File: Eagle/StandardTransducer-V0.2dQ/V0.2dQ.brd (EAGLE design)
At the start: 59.2 x 58 mm, 72 parts, among them CON1 SPI, IC2 TL072D, IC3 LP5907, IC4 LORA-RA_01_SOIC, J1 87758-0216, Q1 FDN340P, Q2 FDN340P, Q3 FDN340P, Q4 FDN340P, Q5 BSP75N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

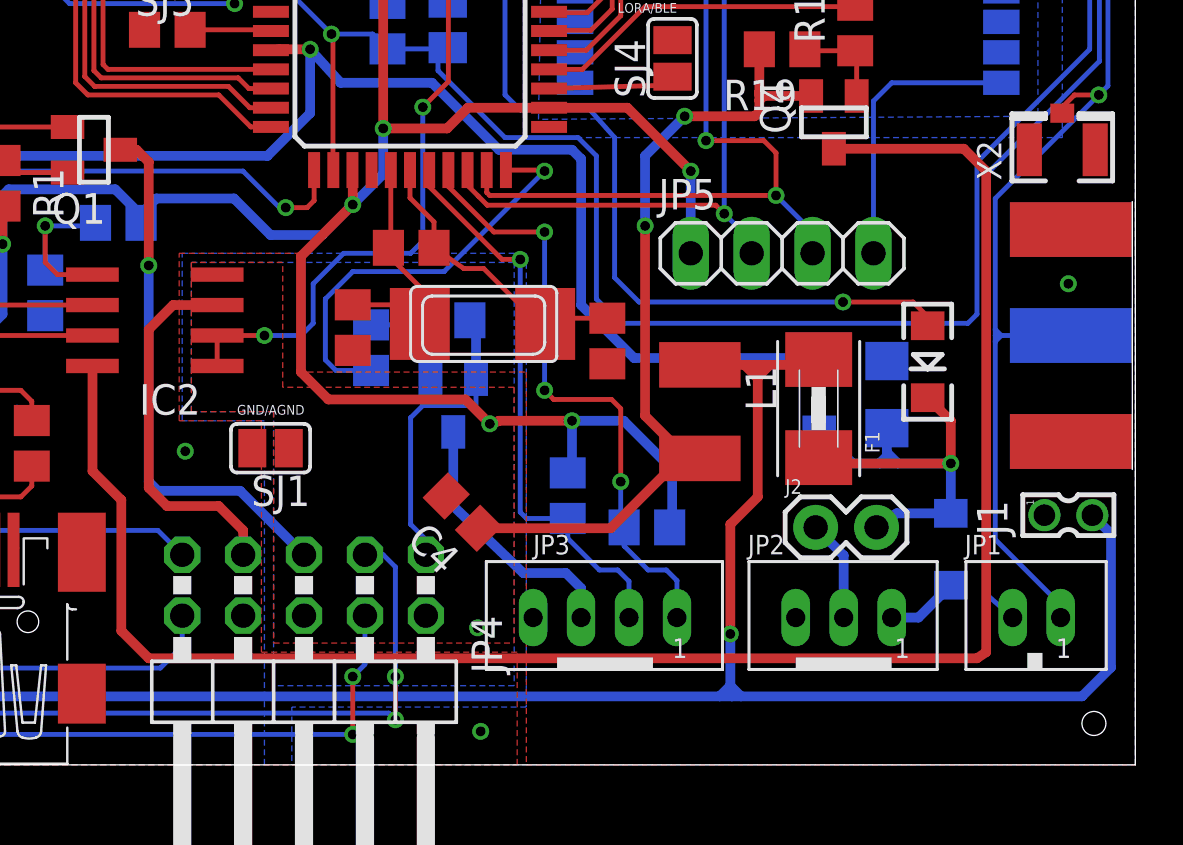
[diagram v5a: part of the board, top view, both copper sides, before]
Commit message: Update ICs, change routes and power source.
Changes made:
- BSP75 (BSP613P) to BSP75N.
- FDN 360P to FDN340P (logic level).
- LP298SX to LP5907 (250 mA).
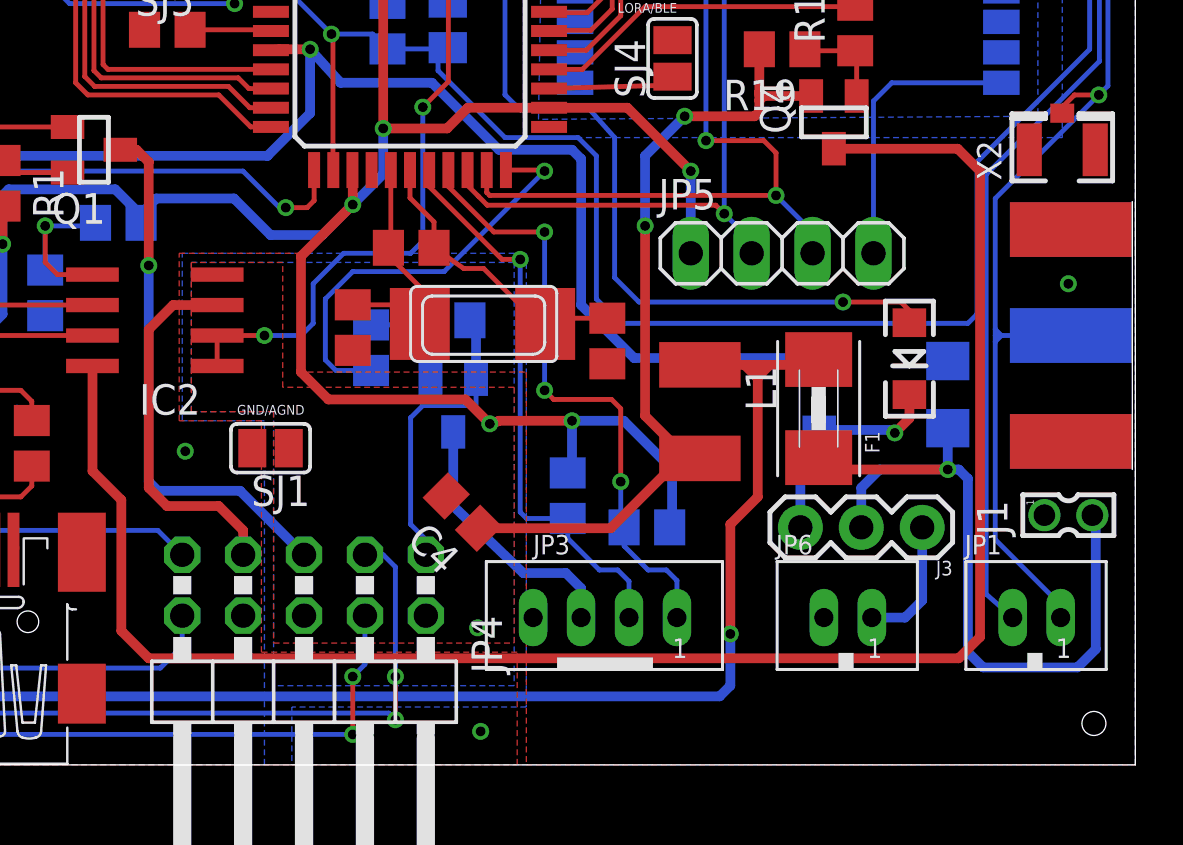
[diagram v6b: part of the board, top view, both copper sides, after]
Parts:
- removed D3: 1N581D1206, lpatiny:LED-1206
- removed J2: (no value), SparkFun-Connectors:1X02
- removed JP2: JST-PH_3-PIN_HEADER, SRG:JST_B3B-PH_HEADER
- added J3: 455-1750-1-ND, SparkFun-Connectors:1X03
- added JP6: JST-PH_2-PIN_HEADER, SRG:JST_B2B-PH_HEADER
- moved C10 2.54 mm to (51.4, 15.4)
- moved D2 0.77 mm to (49.8, 16.9)
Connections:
- removed net +3V3: J2.1, JP2.P2
- new net N$2: D2.C, D4.C, J3.3
- net GND: now also JP6.P2; no longer JP2.P3
- net VCC: now also J1.2, J3.2; no longer D2.C, D3.C, D4.C, J2.2
- net VDD: now also J3.1, JP6.P1; no longer D3.A, JP2.P1
- net VIN: no longer J1.2
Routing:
- net VIN: track 151.0 -> 126.4 mm
- net VCC: track 22.4 -> 32.7 mm
- net N$2: track 0.00 -> 9.44 mm, vias 0 -> 1
- net +3V3: track 4.25 -> 0.00 mm
- net VDD: track 3.10 -> 5.44 mm
- net AVCCOPA: track 75.0 -> 74.1 mm
- net ISP+5V: track 47.0 -> 46.2 mm
